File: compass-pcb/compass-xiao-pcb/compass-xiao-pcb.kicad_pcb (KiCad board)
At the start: 2 copper layers, 186.5 x 72.9 mm, 45 parts

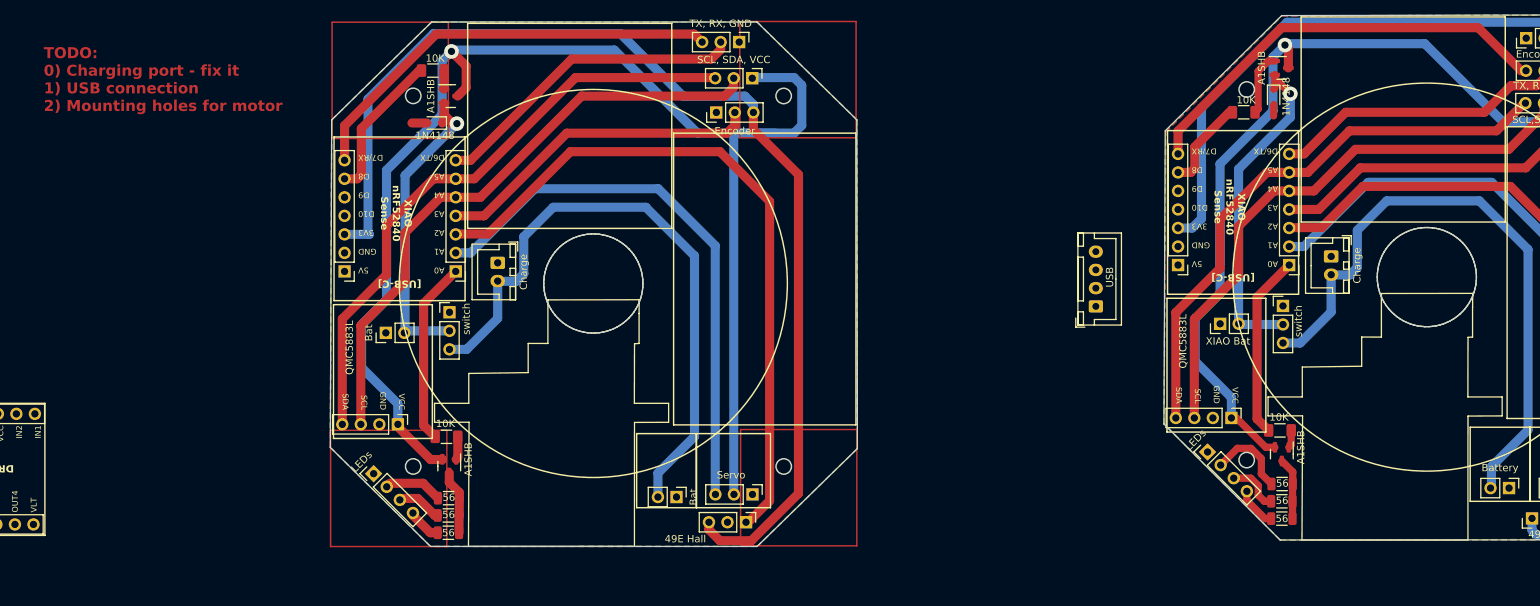
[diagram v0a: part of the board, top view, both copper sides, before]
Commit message: added large USB/charging port
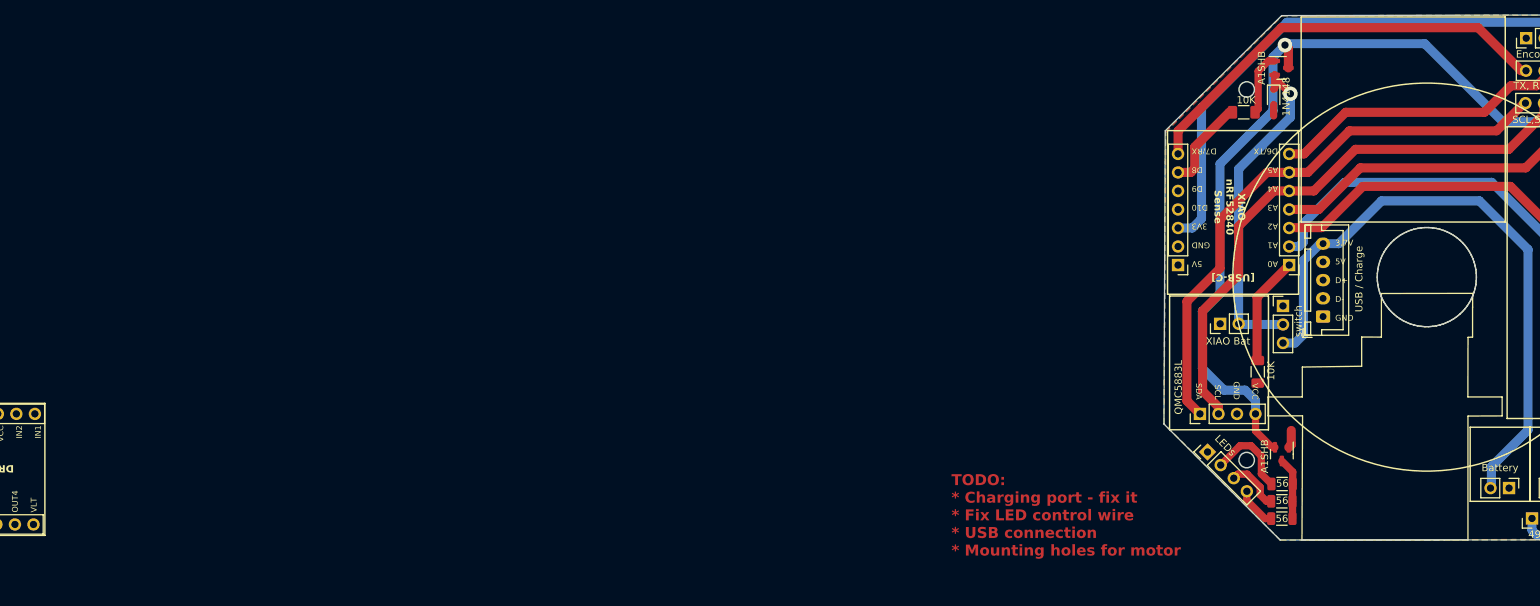
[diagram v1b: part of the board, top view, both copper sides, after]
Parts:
- removed the 10K at (93.3, 97.8)
- removed the 10K at (91.4, 47.6)
- removed the 1N4148 at (91.7, 54.8)
- removed the 49E Hall at (134.4, 109.5)
- removed the 56 at (93.6, 108.6)
- removed the 56 at (93.6, 111.0)
- removed the 56 at (93.6, 106.2)
- removed the A1SHB at (93.7, 101.9)
- removed the A1SHB at (93.9, 51.1)
- removed Bat (x2): PinHeader_1x02_P2.54mm_Vertical, Connector_PinHeader_2.54mm:PinHeader_1x02_P2.54mm_Vertical
- removed Charge (x2): Charger, Connector_JST:JST_XH_B2B-XH-A_1x02_P2.50mm_Vertical
- removed the LEDs at (83.3, 102.9)
- removed the QMC5883L at (86.7, 96.1)
- removed the REF** at (135.2, 48.7)
- removed the REF** at (94.6, 75.2)
- removed the REF** at (79.3, 75.2)
- removed the REF** at (133.5, 43.7)
- removed the REF** at (130.3, 53.4)
- removed the Servo at (135.3, 105.7)
- removed USB: JST_XH_B4B-XH-A_1x04_P2.50mm_Vertical, Connector_JST:JST_XH_B4B-XH-A_1x04_P2.50mm_Vertical
- removed the switch at (93.7, 80.8)
- added USB / Charge: JST_XH_B5B-XH-A_1x05_P2.50mm_Vertical, Connector_JST:JST_XH_B5B-XH-A_1x05_P2.50mm_Vertical, F.Cu at (213.5, 81.4)
- moved 10K 8.60 mm to (204.6, 88.9), turned to 90 degrees
- moved QMC5883L 4.35 mm to (196.6, 94.7), turned to 90 degrees
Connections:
- QMC5883L pad 2: GND -> (no net)
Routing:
- net (no net): track 2059.0 -> 1004.5 mm, vias 4 -> 2
- net GND: track 3.62 -> 1.55 mm
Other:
- board size 186.5 x 72.9 mm -> 72.2 x 72 mm
- board text added: "3.7V 5V D+ D- GND"
- board text added: "TODO: * Charging port - fix it * Fix LED control wire * USB connection * Mounting holes for motor"
- board text removed: "TODO: 0) Charging port - fix it 1) USB connection 2) Mounting holes for motor"

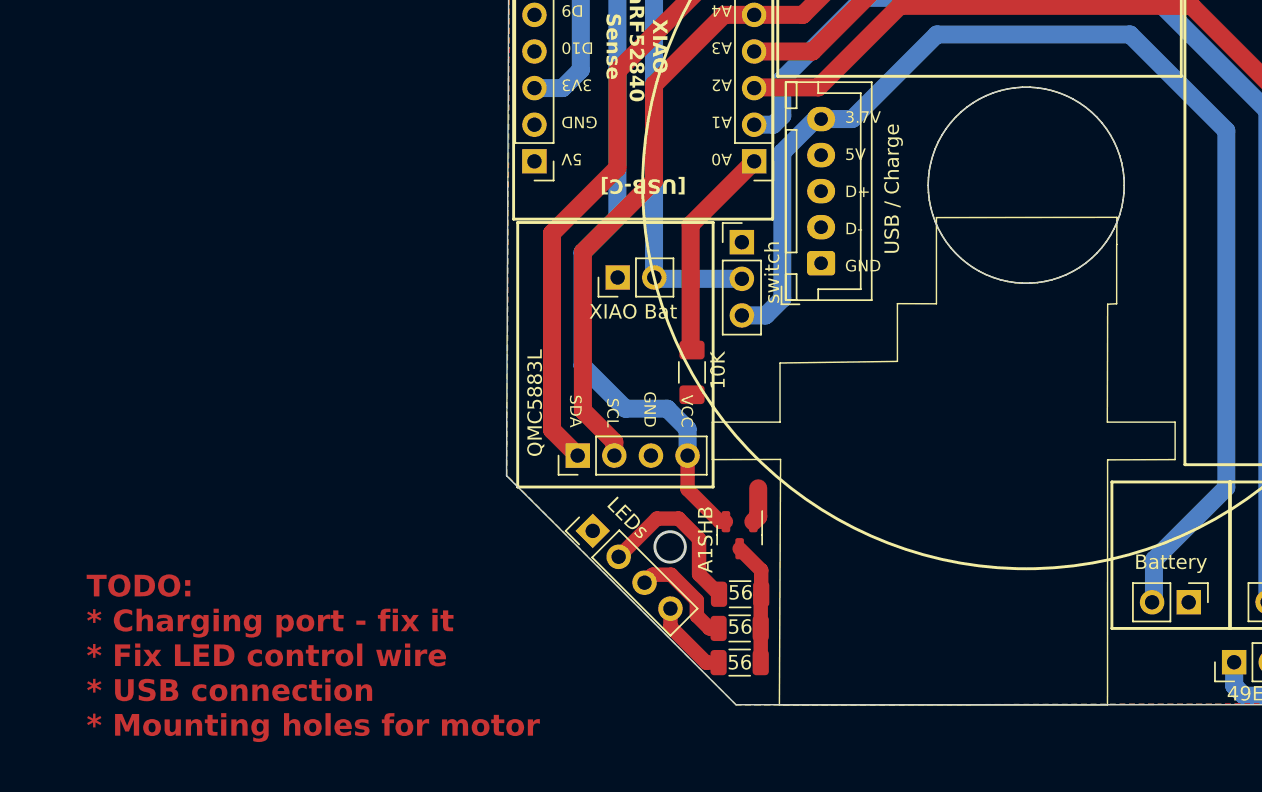
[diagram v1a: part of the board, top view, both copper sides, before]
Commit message: Fixing LED wire, removing some zones
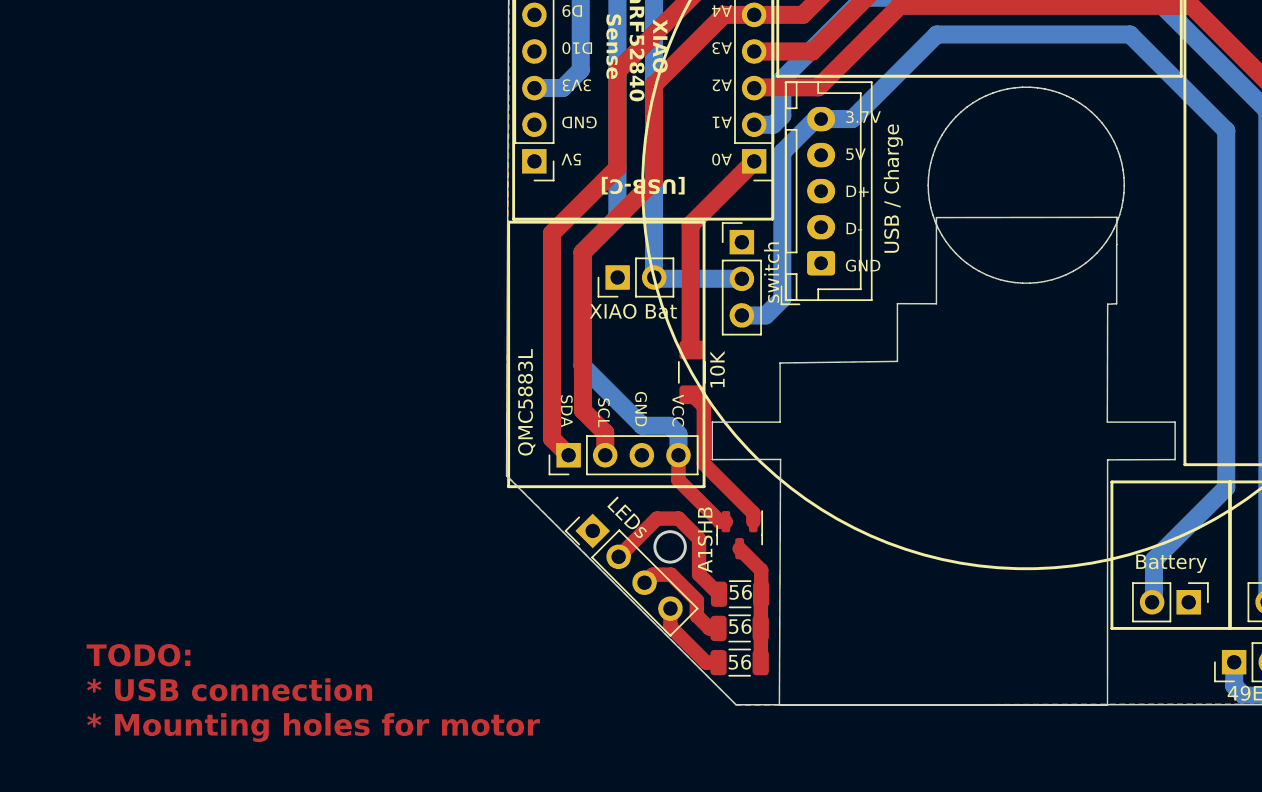
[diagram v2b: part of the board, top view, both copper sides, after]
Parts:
- moved QMC5883L 0.63 mm to (196.0, 94.7)
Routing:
- net (no net): track 1004.5 -> 1011.5 mm
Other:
- outline, holes or cut-outs redrawn
- board text added: "TODO: * USB connection * Mounting holes for motor"
- board text removed: "TODO: * Charging port - fix it * Fix LED control wire * USB connection * Mounting holes for motor"

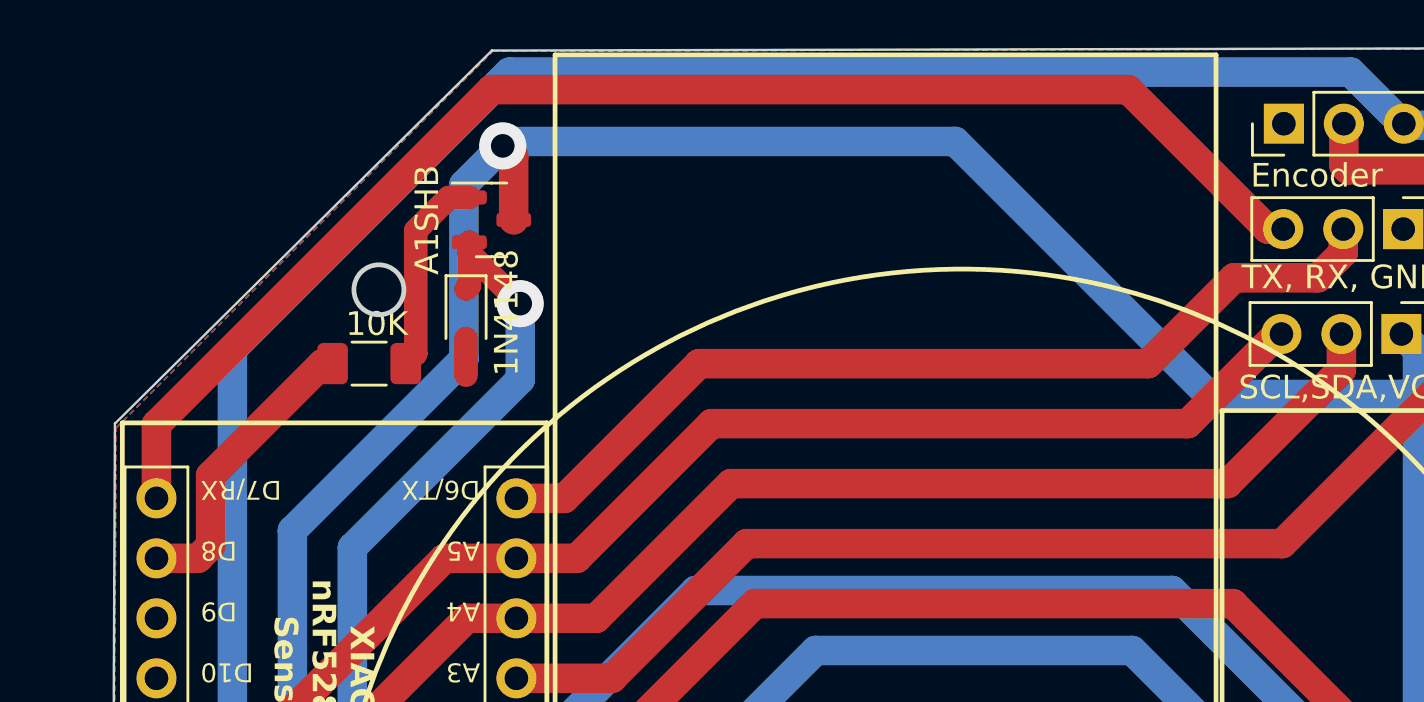
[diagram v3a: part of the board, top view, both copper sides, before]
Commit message: fixing zones around mounting holes
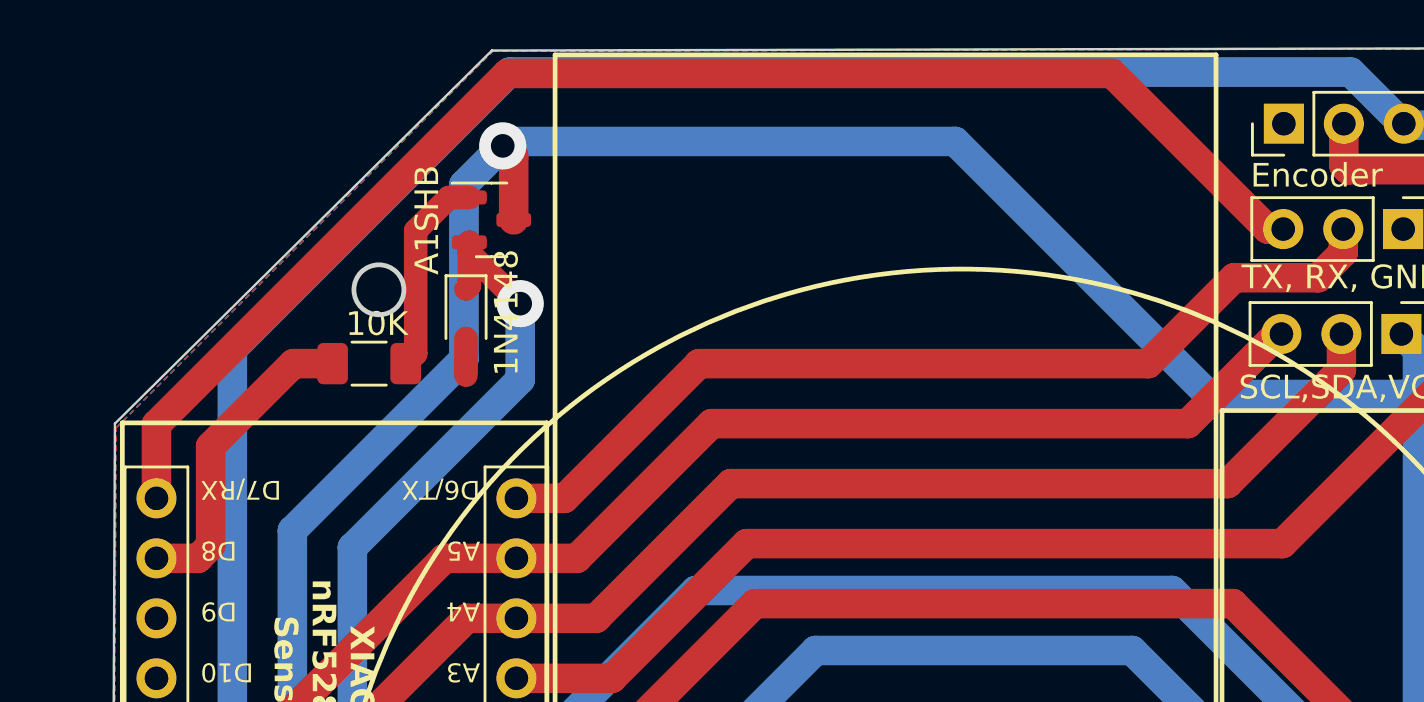
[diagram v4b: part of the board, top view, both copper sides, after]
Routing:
- net (no net): track 1011.5 -> 1012.7 mm

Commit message: corner alignment points
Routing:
- net (no net): track 1012.7 -> 1013.9 mm, vias 2 -> 22

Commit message: mounting holes for motor
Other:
- outline, holes or cut-outs redrawn
- board text added: "TODO: * USB connection pads"
- board text removed: "TODO: * USB connection * Mounting holes for motor"
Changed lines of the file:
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@@
   (gr_rect (start 233.68 96.52) (end 241.870902 106.68)
     (stroke (width 0.2) (type default)) (fill none) (layer "F.SilkS"))
+  (gr_circle locked (center 217.015209 86.36) (end 218.015209 86.36)
+    (stroke (width 0.2) (type default)) (fill none) (layer "Edge.Cuts"))
   (gr_circle (center 253.847056 101.027577) (end 254.905048 101.027577)
     (stroke (width 0.2) (type default)) (fill none) (layer "Edge.Cuts"))
+  (gr_circle locked (center 235.178837 86.345322) (end 236.178837 86.345322)
+    (stroke (width 0.2) (type default)) (fill none) (layer "Edge.Cuts"))
   (gr_circle (center 203.03897 101.025815) (end 204.096962 101.025815)
+    (stroke (width 0.2) (type default)) (fill none) (layer "Edge.Cuts"))
+  (gr_circle locked (center 234.038862 70) (end 235.038862 70)
     (stroke (width 0.2) (type default)) (fill none) (layer "Edge.Cuts"))
   (gr_poly locked
@@
     )
     (stroke (width 0.1) (type solid)) (fill none) (layer "Edge.Cuts"))
+  (gr_circle locked (center 221.461261 70) (end 222.461261 70)
+    (stroke (width 0.2) (type default)) (fill none) (layer "Edge.Cuts"))
   (gr_circle (center 253.834865 50.228125) (end 254.892857 50.228125)
     (stroke (width 0.2) (type default)) (fill none) (layer "Edge.Cuts"))
-  (gr_text "TODO:\n* USB connection\n* Mounting holes for motor" (at 162.56 114.3) (layer "F.Cu")
+  (gr_text "TODO:\n* USB connection pads" (at 162.56 114.3) (layer "F.Cu")
     (effects (font (size 1.5 1.5) (thickness 0.3) bold) (justify left bottom))
   )
@@
   (segment (start 227.447839 43.930822) (end 238.161199 54.644182) (width 1.25) (layer "B.Cu") (net 0))
   (segment (start 206.735185 52.278896) (end 206.735185 53.830275) (width 1) (layer "F.Cu") (net 1))
+  (zone locked (net 0) (net_name "") (layer "F.Cu") (hatch edge 0.5)
+    (connect_pads (clearance 0))
+    (min_thickness 1) (filled_areas_thickness no)
+    (keepout (tracks not_allowed) (vias not_allowed) (pads not_allowed) (copperpour not_allowed) (footprints allowed))
+    (fill (thermal_gap 0.5) (thermal_bridge_width 1) (island_removal_mode 1) (island_area_min 10))
+    (polygon
+      (pts
+        (xy 236.178837 86.345322)
+        (xy 236.159622 86.150232)
+        (xy 236.102717 85.962639)
+        (xy 236.010307 85.789752)
+        (xy 235.885944 85.638215)
+        (xy 235.734407 85.513852)
+        (xy 235.56152 85.421442)
+        (xy 235.373927 85.364537)
+        (xy 235.178837 85.345322)
+        (xy 234.983747 85.364537)
+        (xy 234.796154 85.421442)
+        (xy 234.623267 85.513852)
+        (xy 234.47173 85.638215)
+        (xy 234.347367 85.789752)
+        (xy 234.254957 85.962639)
+        (xy 234.198052 86.150232)
+        (xy 234.178837 86.345322)
+        (xy 234.198052 86.540412)
+        (xy 234.254957 86.728005)
+        (xy 234.347367 86.900892)
+        (xy 234.47173 87.052429)
+        (xy 234.623267 87.176792)
+        (xy 234.796154 87.269202)
+        (xy 234.983747 87.326107)
+        (xy 235.178837 87.345322)
+        (xy 235.373927 87.326107)
+        (xy 235.56152 87.269202)
+        (xy 235.734407 87.176792)
+        (xy 235.885944 87.052429)
+        (xy 236.010307 86.900892)
+        (xy 236.102717 86.728005)
+        (xy 236.159622 86.540412)
+        (xy 236.178837 86.345322)
+      )
+    )
+  )
+  (zone locked (net 0) (net_name "") (layer "F.Cu") (hatch edge 0.5)
+    (connect_pads (clearance 0))
+    (min_thickness 1) (filled_areas_thickness no)
+    (keepout (tracks not_allowed) (vias not_allowed) (pads not_allowed) (copperpour not_allowed) (footprints allowed))
+    (fill (thermal_gap 0.5) (thermal_bridge_width 1) (island_removal_mode 1) (island_area_min 10))
+    (polygon
+      (pts
+        (xy 218.043187 86.36)
+        (xy 218.023972 86.16491)
+        (xy 217.967067 85.977317)
+        (xy 217.874657 85.80443)
+        (xy 217.750294 85.652893)
+        (xy 217.598757 85.52853)
+        (xy 217.42587 85.43612)
+        (xy 217.238277 85.379215)
+        (xy 217.043187 85.36)
+        (xy 216.848097 85.379215)
+        (xy 216.660504 85.43612)
+        (xy 216.487617 85.52853)
+        (xy 216.33608 85.652893)
+        (xy 216.211717 85.80443)
+        (xy 216.119307 85.977317)
+        (xy 216.062402 86.16491)
+        (xy 216.043187 86.36)
+        (xy 216.062402 86.55509)
+        (xy 216.119307 86.742683)
+        (xy 216.211717 86.91557)
+        (xy 216.33608 87.067107)
+        (xy 216.487617 87.19147)
+        (xy 216.660504 87.28388)
+        (xy 216.848097 87.340785)
+        (xy 217.043187 87.36)
+        (xy 217.238277 87.340785)
+        (xy 217.42587 87.28388)
+        (xy 217.598757 87.19147)
+        (xy 217.750294 87.067107)
+        (xy 217.874657 86.91557)
+        (xy 217.967067 86.742683)
+        (xy 218.023972 86.55509)
+        (xy 218.043187 86.36)
+      )
+    )
+  )
+  (zone locked (net 0) (net_name "") (layer "F.Cu") (hatch edge 0.5)
+    (connect_pads (clearance 0))
+    (min_thickness 1) (filled_areas_thickness no)
+    (keepout (tracks not_allowed) (vias not_allowed) (pads not_allowed) (copperpour not_allowed) (footprints not_allowed))
+    (fill (thermal_gap 0.5) (thermal_bridge_width 1) (island_removal_mode 1) (island_area_min 10))
+    (polygon
+      (pts
+        (xy 222.464515 70.032687)
+        (xy 222.4453 69.837597)
+        (xy 222.388395 69.650004)
+        (xy 222.295985 69.477117)
+        (xy 222.171622 69.32558)
+        (xy 222.020085 69.201217)
+        (xy 221.847198 69.108807)
+        (xy 221.659605 69.051902)
+        (xy 221.464515 69.032687)
+        (xy 221.269425 69.051902)
+        (xy 221.081832 69.108807)
+        (xy 220.908945 69.201217)
+        (xy 220.757408 69.32558)
+        (xy 220.633045 69.477117)
+        (xy 220.540635 69.650004)
+        (xy 220.48373 69.837597)
+        (xy 220.464515 70.032687)
+        (xy 220.48373 70.227777)
+        (xy 220.540635 70.41537)
+        (xy 220.633045 70.588257)
+        (xy 220.757408 70.739794)
+        (xy 220.908945 70.864157)
+        (xy 221.081832 70.956567)
+        (xy 221.269425 71.013472)
+        (xy 221.464515 71.032687)
+        (xy 221.659605 71.013472)
+        (xy 221.847198 70.956567)
+        (xy 222.020085 70.864157)
+        (xy 222.171622 70.739794)
+        (xy 222.295985 70.588257)
+        (xy 222.388395 70.41537)
+        (xy 222.4453 70.227777)
+        (xy 222.464515 70.032687)
+      )
+    )
+  )
+  (zone locked (net 0) (net_name "") (layer "F.Cu") (hatch edge 0.5)
+    (connect_pads (clearance 0))
+    (min_thickness 1) (filled_areas_thickness no)
+    (keepout (tracks not_allowed) (vias not_allowed) (pads not_allowed) (copperpour not_allowed) (footprints allowed))
+    (fill (thermal_gap 0.5) (thermal_bridge_width 1) (island_removal_mode 1) (island_area_min 10))
+    (polygon
+      (pts
+        (xy 235.040832 70.032687)
+        (xy 235.021617 69.837597)
+        (xy 234.964712 69.650004)
+        (xy 234.872302 69.477117)
+        (xy 234.747939 69.32558)
+        (xy 234.596402 69.201217)
+        (xy 234.423515 69.108807)
+        (xy 234.235922 69.051902)
+        (xy 234.040832 69.032687)
+        (xy 233.845742 69.051902)
+        (xy 233.658149 69.108807)
+        (xy 233.485262 69.201217)
+        (xy 233.333725 69.32558)
+        (xy 233.209362 69.477117)
+        (xy 233.116952 69.650004)
+        (xy 233.060047 69.837597)
+        (xy 233.040832 70.032687)
+        (xy 233.060047 70.227777)
+        (xy 233.116952 70.41537)
+        (xy 233.209362 70.588257)
+        (xy 233.333725 70.739794)
+        (xy 233.485262 70.864157)
+        (xy 233.658149 70.956567)
+        (xy 233.845742 71.013472)
+        (xy 234.040832 71.032687)
+        (xy 234.235922 71.013472)
+        (xy 234.423515 70.956567)
+        (xy 234.596402 70.864157)
+        (xy 234.747939 70.739794)
+        (xy 234.872302 70.588257)
+        (xy 234.964712 70.41537)
+        (xy 235.021617 70.227777)
+        (xy 235.040832 70.032687)
+      )
+    )
+  )
   (zone locked (net 0) (net_name "") (layers "F&B.Cu") (hatch edge 0.5)
     (connect_pads (clearance 0))

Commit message: polishing
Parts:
- moved 10K 8.61 mm to (207.9, 96.8), turned to 180 degrees
- moved A1SHB 0.29 mm to (207.9, 100.5)
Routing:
- net (no net): track 1013.9 -> 1030.8 mm
